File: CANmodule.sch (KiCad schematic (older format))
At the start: 16 parts, among them J201 RJ45, J202 RJ45, U201 TLP2361, U202 TLP2361, U203 MCP2551-I/SN

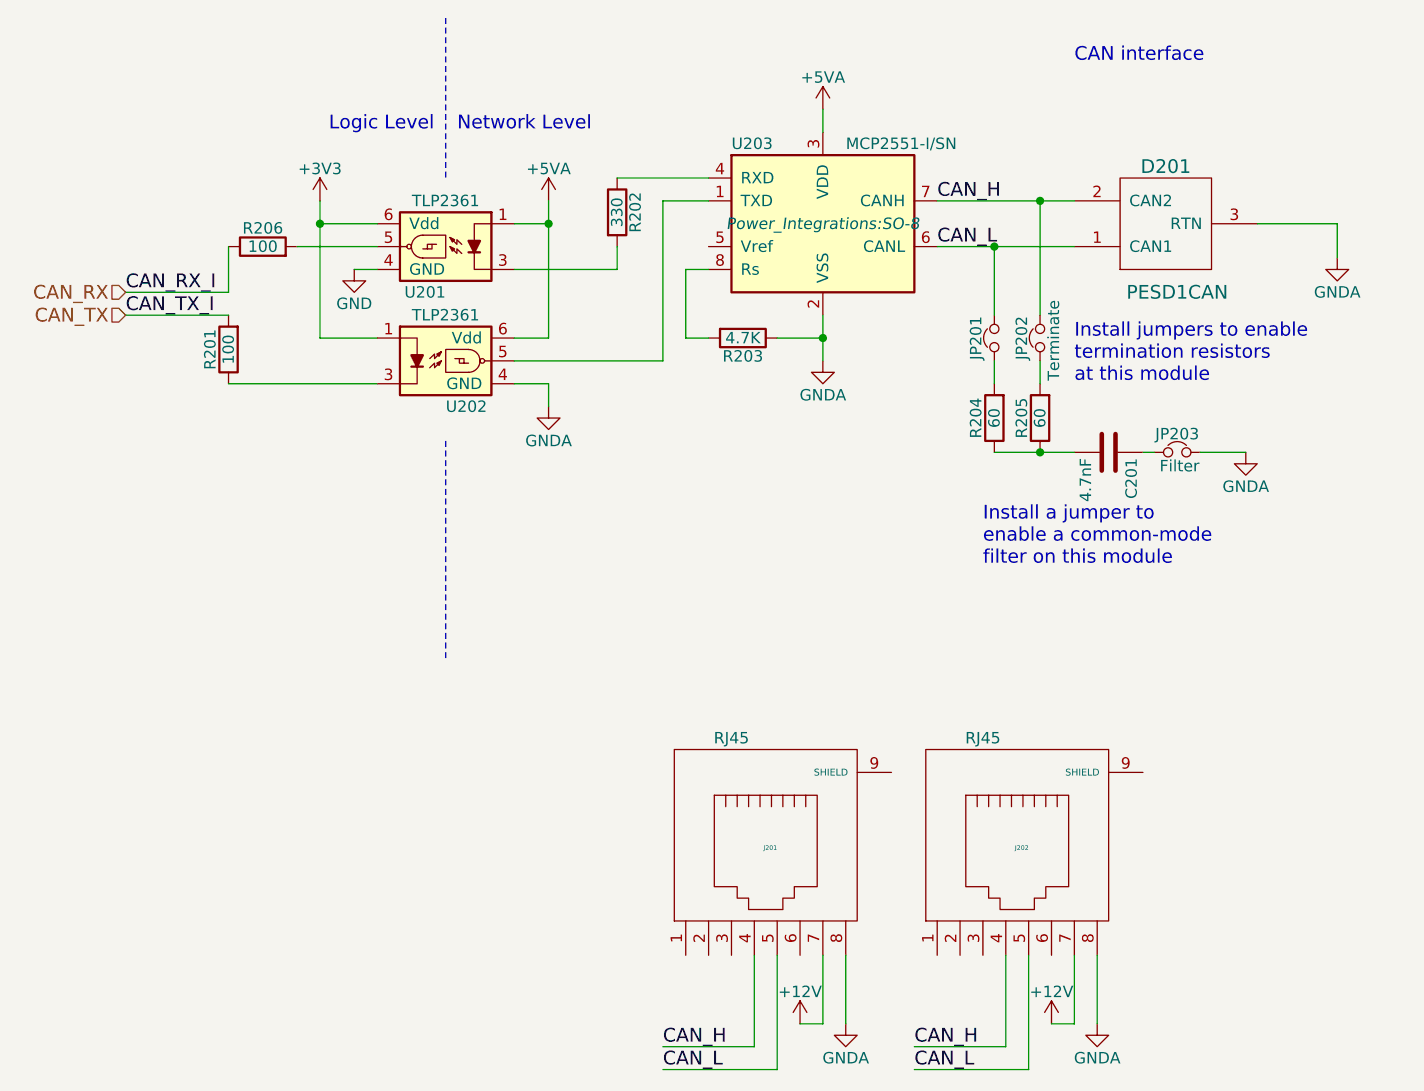
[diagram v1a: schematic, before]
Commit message: pour and silk edits
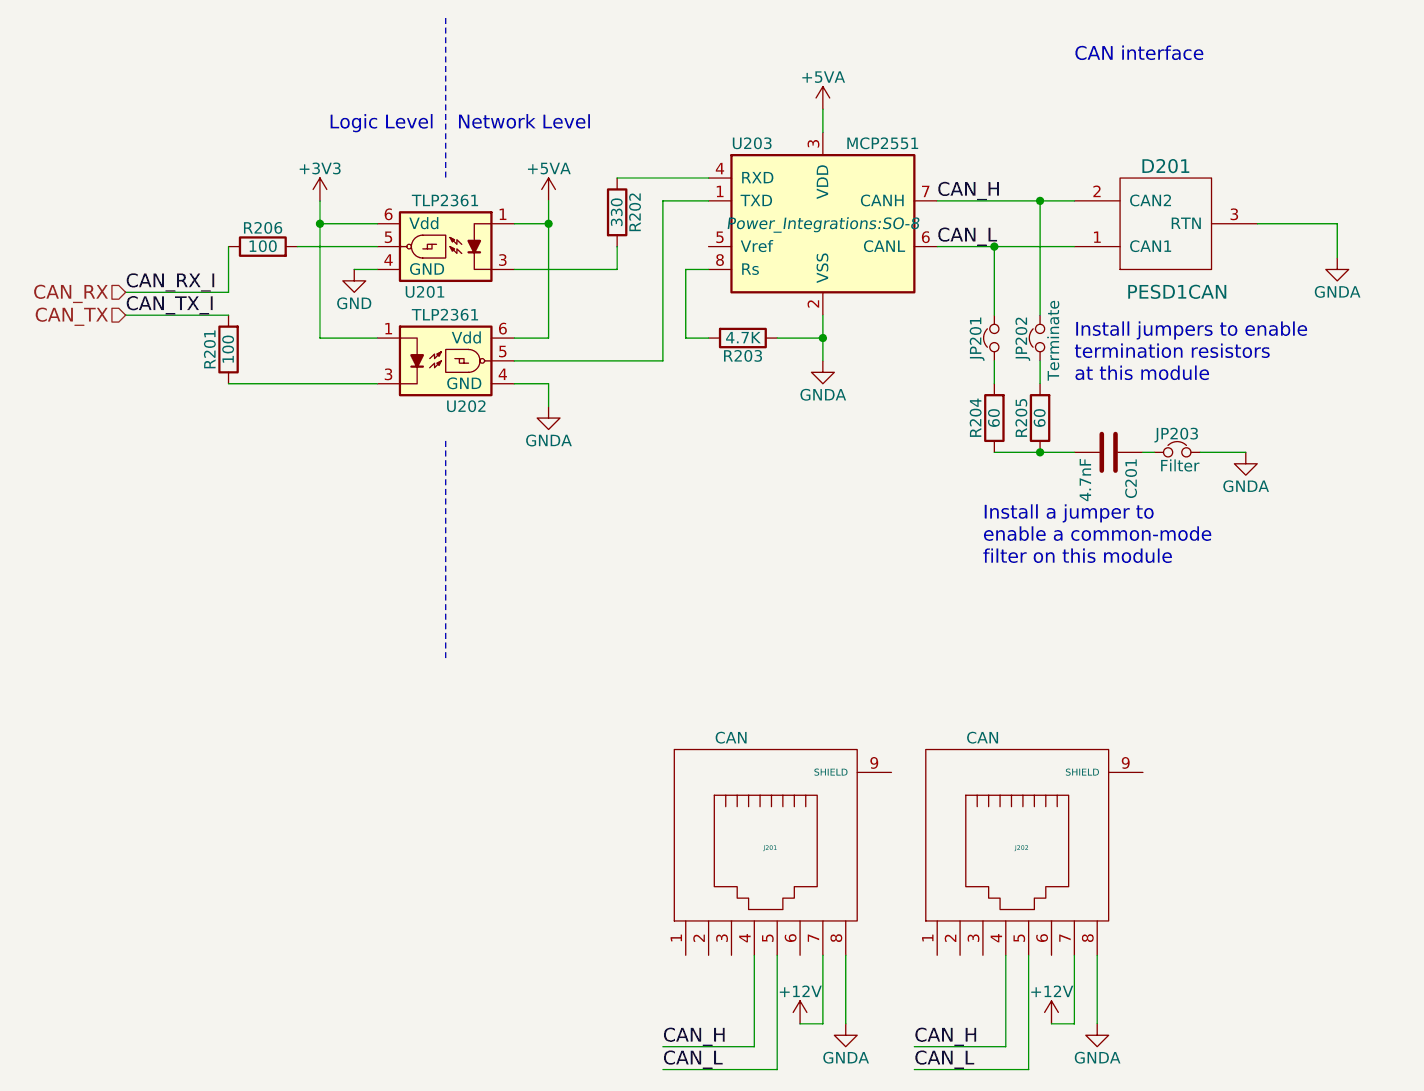
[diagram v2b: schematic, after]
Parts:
- J201, J202: value RJ45 -> CAN
- U203: value MCP2551-I/SN -> MCP2551
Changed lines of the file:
@@
 P 7200 1500
 F 0 "U203" H 6800 1850 50  0000 L CNN
-F 1 "MCP2551-I/SN" H 7300 1850 50  0000 L CNN
+F 1 "MCP2551" H 7300 1850 50  0000 L CNN
 F 2 "Power_Integrations:SO-8" H 7200 1500 50  0000 C CIN
 F 3 "" H 7200 1500 50  0000 C CNN
@@
 P 8050 4250
 F 0 "J202" H 8070 4270 20  0000 C CNN
-F 1 "RJ45" H 7900 4750 50  0000 C CNN
+F 1 "CAN" H 7900 4750 50  0000 C CNN
 F 2 "Connect:RJ45_8" H 8050 4250 50  0001 C CNN
 F 3 "" H 8050 4250 50  0000 C CNN
@@
 P 6950 4250
 F 0 "J201" H 6970 4270 20  0000 C CNN
-F 1 "RJ45" H 6800 4750 50  0000 C CNN
+F 1 "CAN" H 6800 4750 50  0000 C CNN
 F 2 "Connect:RJ45_8" H 6950 4250 50  0001 C CNN
 F 3 "" H 6950 4250 50  0000 C CNN
